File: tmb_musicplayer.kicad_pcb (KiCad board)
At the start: 2 copper layers, 99.1 x 95.3 mm, 194 parts, among them J1 SWD, J2 RC522_Header, J3 Screw_Terminal_1x02, P2 VolDown, P3 Prev, P4 Play, P5 Next, P6 VolUp, P7 CONN_02X10, Q1 BSS138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

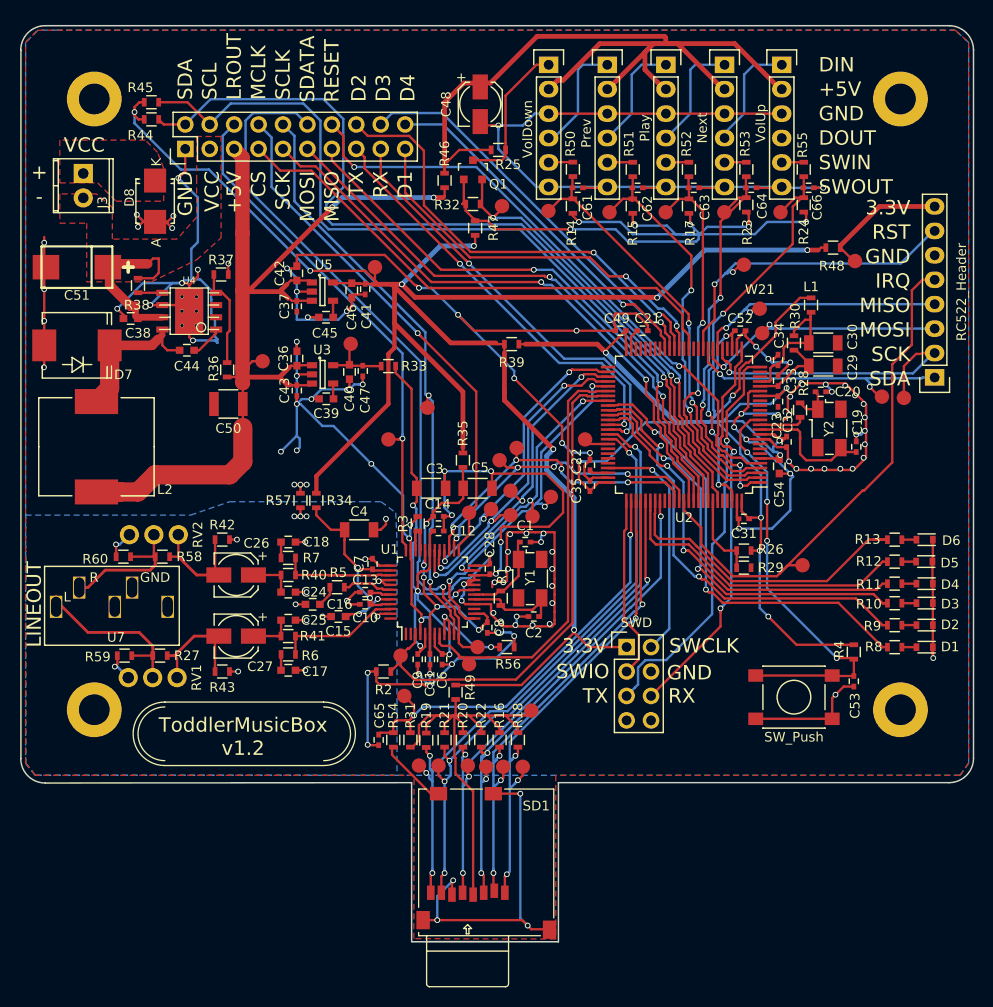
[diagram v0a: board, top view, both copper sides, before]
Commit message: Changed butten connectors
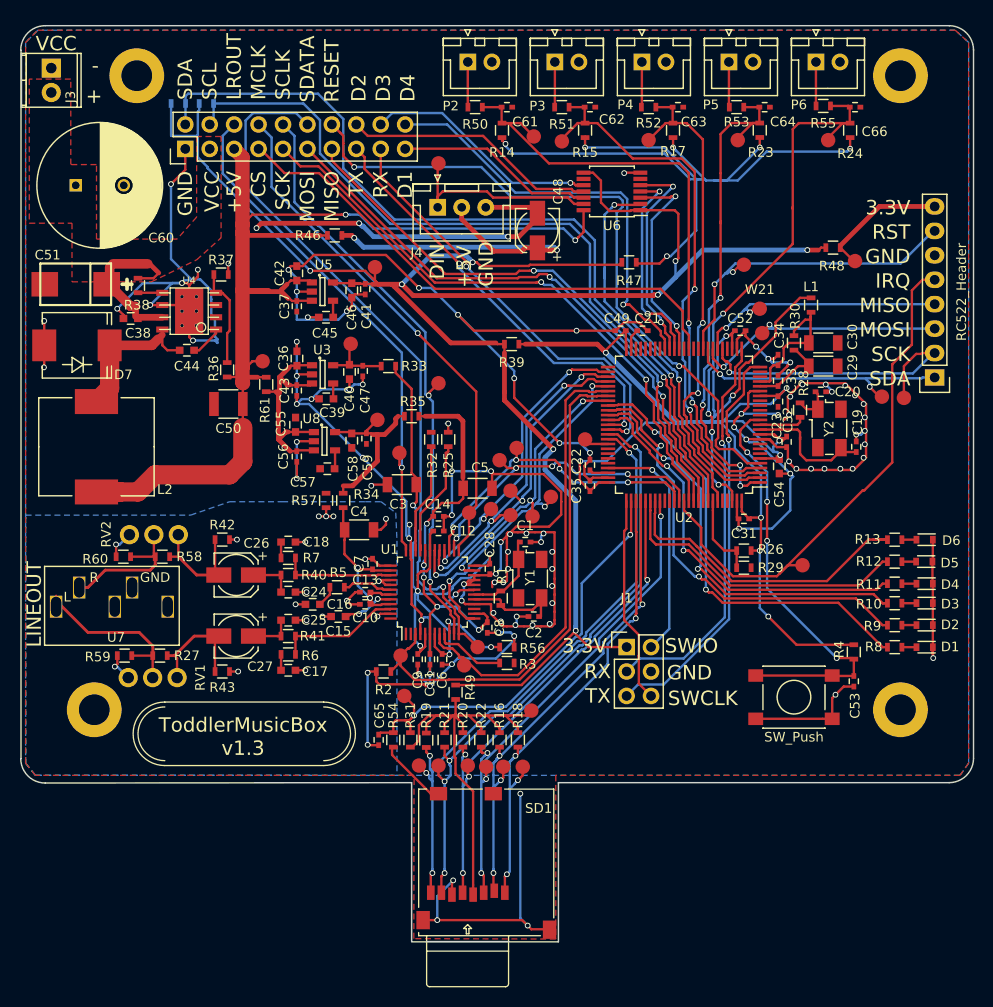
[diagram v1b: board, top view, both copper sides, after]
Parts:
- removed D8: D_Schottky_30_V_3A, Diodes_SMD:SMB_Standard
- removed Q1: BSS138, TO_SOT_Packages_SMD:SOT-23
- added C55: 1uF, Capacitors_SMD:C_0603, F.Cu at (94.6, 92.3)
- added C56: 100nF, Capacitors_SMD:C_0402, F.Cu at (94.7, 95.6)
- added C57: 10nF, Capacitors_SMD:C_0603, F.Cu at (97.9, 96.9)
- added C58: 1uF, Capacitors_SMD:C_0603, F.Cu at (100.4, 93.9)
- added C59: 100nF, Capacitors_SMD:C_0402, F.Cu at (102.0, 93.7)
- added C60: 10uF, Capacitors_THT:C_Radial_D13_L21_P5, F.Cu at (71.7, 67.4)
- added J4: LED, Connectors_JST:JST_XH_B03B-XH-A_03x2.50mm_Straight, F.Cu at (109.4, 69.7)
- added R61: 0, Resistors_SMD:R_0603, F.Cu at (91.5, 88.1)
- added U6: TXB0104, Housings_SSOP:TSSOP-14_4.4x5mm_Pitch0.65mm, F.Cu at (127.5, 68.0)
- added U8: LD3985M33R, TO_SOT_Packages_SMD:SOT-23-5, F.Cu at (97.6, 94.0)
- added W38: 3.3V, Measurement_Points:Measurement_Point_Round-SMD-Pad_Small, F.Cu at (103.1, 91.8)
- J1: footprint Pin_Headers:Pin_Header_Straight_2x04 -> Pin_Headers:Pin_Header_Straight_2x03
- P2, P3, P4, P5, P6: footprint Pin_Headers:Pin_Header_Straight_1x06 -> Connectors_JST:JST_XH_B02B-XH-A_02x2.50mm_Straight
- R25, R32: value 10k -> 100k
- R44, R45: moved to B.Cu
- SD1: footprint MF_Connectors:MF_Connectors-MF-MICROSD -> jfi:MF_Connectors-MF-MICROSD
- moved R25 30.5 mm to (110.5, 93.8), turned to 90 degrees
- moved R32 24.9 mm to (108.7, 93.8), turned to 90 degrees
- moved R3 17.2 mm to (116.6, 117.1), turned to 0 degrees
- moved R47 16.4 mm to (129.3, 75.4), turned to 180 degrees
- moved C48 14.4 mm to (119.7, 72.1), turned to 90 degrees
- moved R46 12.8 mm to (98.7, 72.6), turned to 0 degrees
- moved R50 12.0 mm to (113.3, 59.3), turned to 0 degrees
- moved J3 11.5 mm to (69.2, 55.2)
- moved C61 11.2 mm to (116.6, 59.3)
- moved R14 10.8 mm to (116.1, 61.7)
- moved R51 9.81 mm to (122.3, 59.3), turned to 0 degrees
- moved C62 9.74 mm to (125.2, 59.3)
- moved C66 9.67 mm to (152.8, 59.3)
- moved R15 9.30 mm to (124.7, 61.7)
- moved R24 9.13 mm to (152.2, 61.7)
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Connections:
- C36 pad 1: +5V -> /Power/+5V_VLSI
- C43 pad 1: +5V -> /Power/+5V_VLSI
- C48 pad 1: /Externals/BTLED_NET_5V -> Net-(C48-Pad1)
- J1 pad 3: /PA14 -> /PA3
- J1 pad 6: /PA3 -> /PA14
- J3 pad 1: Net-(D8-Pad1) -> GND
- P2 pad 2: /Externals/BTLED_NET_5V -> GND
- P3 pad 1: Net-(P2-Pad4) -> Net-(P3-Pad1)
- P3 pad 2: /Externals/BTLED_NET_5V -> GND
- P4 pad 1: Net-(P3-Pad4) -> Net-(P4-Pad1)
- P4 pad 2: /Externals/BTLED_NET_5V -> GND
- P5 pad 1: Net-(P4-Pad4) -> Net-(P5-Pad1)
- P5 pad 2: /Externals/BTLED_NET_5V -> GND
- P6 pad 1: Net-(P5-Pad4) -> Net-(P6-Pad1)
- P6 pad 2: /Externals/BTLED_NET_5V -> GND
- P7 pad 16: /PE9 -> /Externals/EXT_DIO2_5V
- P7 pad 18: /PE10 -> /Externals/EXT_DIO3_5V
- P7 pad 19: /PE8 -> /Externals/EXT_DIO1_5V
- R14 pad 1: Net-(Q1-Pad1) -> Net-(R14-Pad1)
- R15 pad 1: Net-(Q1-Pad1) -> Net-(R14-Pad1)
- R17 pad 1: Net-(Q1-Pad1) -> Net-(R14-Pad1)
- R23 pad 1: Net-(Q1-Pad1) -> Net-(R14-Pad1)
- R24 pad 1: Net-(Q1-Pad1) -> Net-(R14-Pad1)
- R25 pad 1: /Externals/BTLED_NET_5V -> Net-(R25-Pad1)
- R25 pad 2: Net-(P2-Pad1) -> GND
- R32 pad 1: Net-(Q1-Pad1) -> Net-(R32-Pad1)
- R32 pad 2: /PB8 -> GND
- R34 pad 2: +3V3 -> +3.3VA
- R35 pad 2: +3V3 -> +3.3VA
- R46 pad 1: /Externals/BTLED_NET_5V -> +5V
- R46 pad 2: +5V -> Net-(C48-Pad1)
- R47 pad 1: Net-(Q1-Pad1) -> Net-(R14-Pad1)
- R50 pad 1: Net-(P2-Pad5) -> Net-(P2-Pad1)
- R51 pad 1: Net-(P3-Pad5) -> Net-(P3-Pad1)
- R52 pad 1: Net-(P4-Pad5) -> Net-(P4-Pad1)
- R53 pad 1: Net-(P5-Pad5) -> Net-(P5-Pad1)
- R55 pad 1: Net-(P6-Pad5) -> Net-(P6-Pad1)
- SD1 pad 10: GND -> Net-(SD1-Pad10)
- U1 pad 33: Net-(R3-Pad1) -> Net-(R25-Pad1)
- U1 pad 34: Net-(R3-Pad1) -> Net-(R32-Pad1)
- U1 pad 9: Net-(R56-Pad1) -> Net-(R3-Pad1)
- U3 pad 1: +5V -> /Power/+5V_VLSI
- U3 pad 3: +5V -> /Power/+5V_VLSI
- W14 pad 1: /PB8 -> /Externals/LED_DATA_5V
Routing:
- net /Externals/BTLED_NET_5V: track 92.5 -> 0.00 mm
- net Net-(R14-Pad1): track 0.00 -> 81.8 mm, vias 0 -> 6
- net Net-(Q1-Pad1): track 76.4 -> 0.00 mm, vias 6 -> 0
- net GND: track 587.6 -> 518.4 mm, vias 109 -> 104
- net Net-(C48-Pad1): track 0.00 -> 35.7 mm, vias 0 -> 2
- net /Externals/EXT_DIO2_5V: track 0.00 -> 26.7 mm
- net /PE9: track 47.4 -> 21.6 mm
- net /Power/+5V_VLSI: track 0.00 -> 24.9 mm
- net /Externals/EXT_DIO3_5V: track 0.00 -> 24.7 mm, vias 0 -> 1
- net /Externals/LED_DATA_5V: track 0.00 -> 21.7 mm
- net /PE5: track 43.8 -> 65.2 mm
- net /Externals/EXT_DIO1_5V: track 0.00 -> 20.9 mm
- net /PE8: track 41.3 -> 21.8 mm
- net /PE10: track 41.8 -> 22.5 mm, vias 1 -> 2
- net +3.3VA: track 0.00 -> 18.4 mm
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- removed copper zone on F.Cu, net Net-(D8-Pad1)
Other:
- board text added: "ToddlerMusicBox v1.3"
- board text removed: "DOUT"
- board text removed: "SWIN"
- board text removed: "SWOUT"
- board text removed: "ToddlerMusicBox v1.2"
